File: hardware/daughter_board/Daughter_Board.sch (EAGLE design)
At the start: 60 parts, among them IC1 LMV358MMX, IC2 LMV358MMX, IC3 ATMEGA2560-16AU, IC5 LMV358MMX, IC8 LMV358MMX, IC9 LMV358MMX, Q1 BSS138, Y1 CSTCE16M0V53-R0 16MHZ

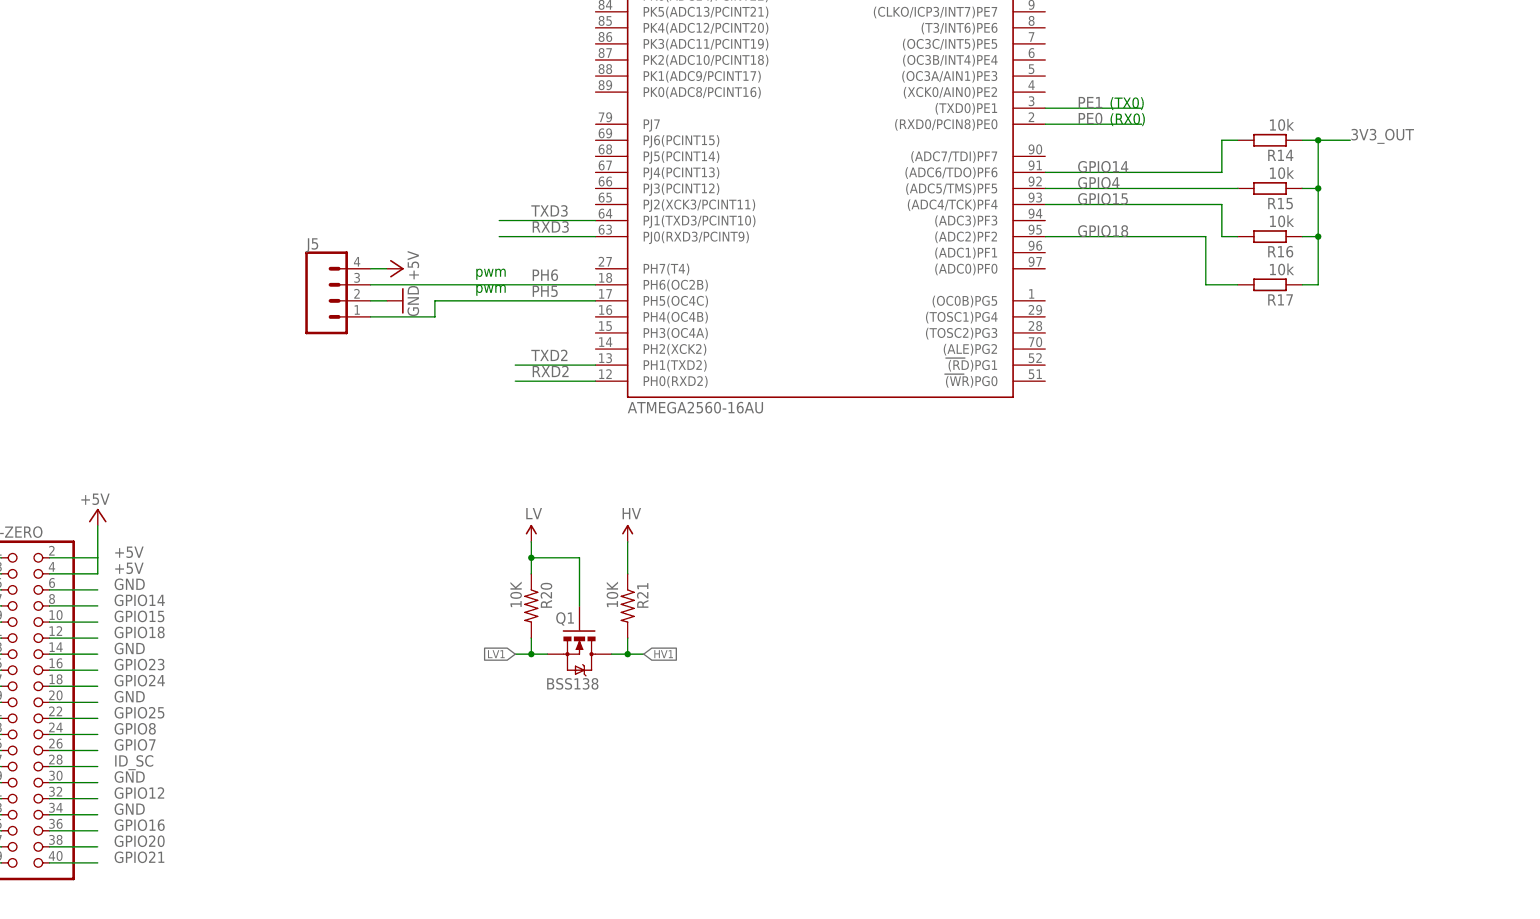
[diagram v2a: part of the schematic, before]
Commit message: level converter and labels
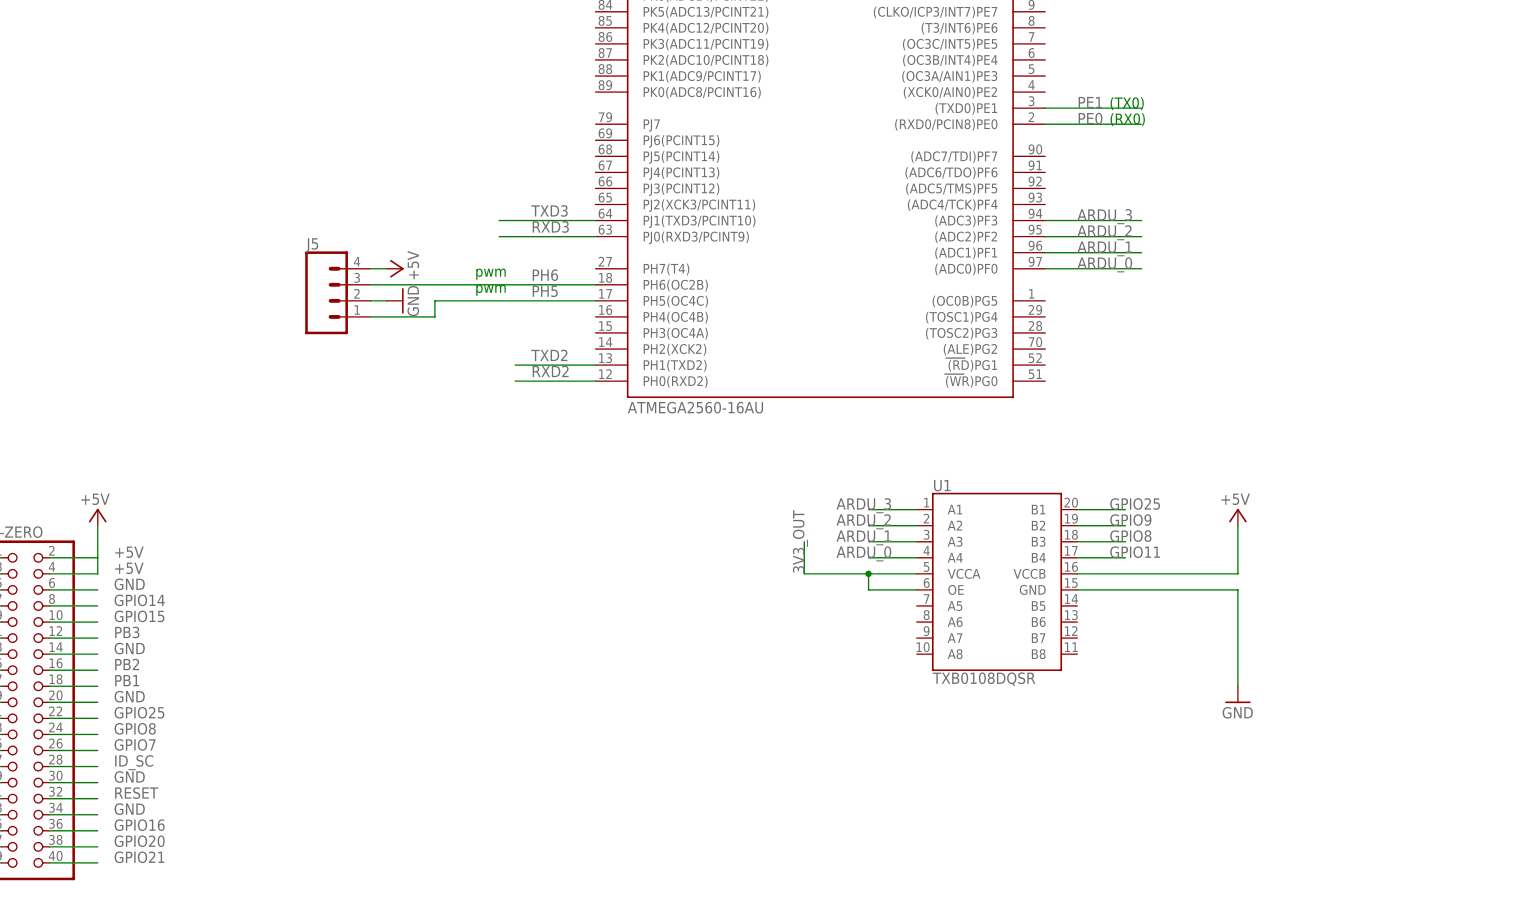
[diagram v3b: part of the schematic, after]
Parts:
- removed Q1: BSS138, SparkFun:MOSFET-NCHANNELSMD
- removed R14, R15, R16, R17: 10k, resistor:R-EU_R0603
- removed R20, R21: 10K, SparkFun:RESISTOR0603-RES
- added U1: TXB0108DQSR, SparkFun-IC-Comms:TXB0108
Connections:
- removed net GPIO12: RPI-ZERO.32
- removed net GPIO18: IC3.(ADC2)PF2, R17.2, RPI-ZERO.12
- removed net GPIO23: RPI-ZERO.16
- removed net GPIO24: RPI-ZERO.18
- removed net HV: R21.1
- removed net HV1: Q1.D, R21.2
- removed net LV: Q1.G, R20.1
- removed net LV1: Q1.S, R20.2
- new net ARDU_0: IC3.(ADC0)PF0, U1.A4
- new net ARDU_1: IC3.(ADC1)PF1, U1.A3
- new net ARDU_2: IC3.(ADC2)PF2, U1.A2
- new net ARDU_3: IC3.(ADC3)PF3, U1.A1
- net +5V: now also U1.VCCB
- net 3V3_OUT: now also U1.OE, U1.VCCA; no longer R14.1, R15.1, R16.1, R17.1
- net GND: now also U1.GND
- net GPIO11: now also U1.B4
- net GPIO14: no longer IC3.(ADC6/TDO)PF6, R14.2
- net GPIO15: no longer IC3.(ADC4/TCK)PF4, R16.2
- net GPIO25: now also U1.B1
- net GPIO4: no longer IC3.(ADC5/TMS)PF5, R15.2
- net GPIO8: now also U1.B3
- net GPIO9: now also U1.B2
- net PB1: now also RPI-ZERO.18
- net PB2: now also RPI-ZERO.16
- net PB3: now also RPI-ZERO.12
- net RESET: now also RPI-ZERO.32

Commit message: some DRC fixes
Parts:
- _: value TS42031-160R-TR-7260 -> TS42
- renumbered RESET to _
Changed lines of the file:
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@@
 <part name="GND20" library="supply1" deviceset="GND" device=""/>
 <part name="R1" library="SmartPrj" deviceset="R-EU_" device="R0603" value="1M"/>
-<part name="RESET" library="SmartPrj" deviceset="TS42" device="" value="TS42031-160R-TR-7260"/>
+<part name="_" library="SmartPrj" deviceset="TS42" device="" value=""/>
 <part name="D3" library="diode" deviceset="DIODE-" device="MINIMELF" value="CD1206-S01575"/>
 <part name="IC1" library="linear" library_urn="urn:adsk.eagle:library:262" deviceset="LMV358?*" device="MM" package3d_urn="urn:adsk.eagle:package:16453/1" technology="X"/>
@@
 <attribute name="VALUE" x="66.675" y="240.792" size="1.778" layer="96" rot="R180"/>
 </instance>
-<instance part="RESET" gate="G$1" x="226.06" y="274.32"/>
+<instance part="_" gate="G$1" x="226.06" y="274.32"/>
 <instance part="D3" gate="G$1" x="256.54" y="287.02" smashed="yes" rot="R90">
 <attribute name="NAME" x="251.9426" y="289.56" size="1.778" layer="95" rot="R270"/>
@@
 <junction x="228.6" y="266.7"/>
 <pinref part="GND12" gate="1" pin="GND"/>
-<pinref part="RESET" gate="G$1" pin="1"/>
-<pinref part="RESET" gate="G$1" pin="2"/>
+<pinref part="_" gate="G$1" pin="1"/>
+<pinref part="_" gate="G$1" pin="2"/>
 </segment>
 <segment>
@@
 <wire x1="228.6" y1="281.94" x2="226.06" y2="281.94" width="0.1524" layer="91"/>
 <wire x1="226.06" y1="281.94" x2="226.06" y2="279.4" width="0.1524" layer="91"/>
-<pinref part="RESET" gate="G$1" pin="4"/>
-<pinref part="RESET" gate="G$1" pin="3"/>
+<pinref part="_" gate="G$1" pin="4"/>
+<pinref part="_" gate="G$1" pin="3"/>
 <wire x1="238.76" y1="276.86" x2="238.76" y2="281.94" width="0.1524" layer="91"/>
 <pinref part="C1" gate="G$1" pin="1"/>

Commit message: Daughter Board v1
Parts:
- removed _: TS42, SmartPrj:TS42
- added S1: MOMENTARY-SWITCH-SPST-SMD-5.2-REDUNDANT, SparkFun-Switches:MOMENTARY-SWITCH-SPST-SMD-5.2-REDUNDANT
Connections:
- net GND: now also S1.1; no longer _.1, _.2
- net RESET: now also S1.2; no longer _.3, _.4
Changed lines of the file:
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@@
 <?xml version="1.0" encoding="utf-8"?>
 <!DOCTYPE eagle SYSTEM "eagle.dtd">
-<eagle version="8.3.2">
+<eagle version="8.4.0">
 <drawing>
 <settings>
@@
 <part name="GND20" library="supply1" deviceset="GND" device=""/>
 <part name="R1" library="SmartPrj" deviceset="R-EU_" device="R0603" value="1M"/>
-<part name="_" library="SmartPrj" deviceset="TS42" device="" value=""/>
 <part name="D3" library="diode" deviceset="DIODE-" device="MINIMELF" value="CD1206-S01575"/>
 <part name="IC1" library="linear" library_urn="urn:adsk.eagle:library:262" deviceset="LMV358?*" device="MM" package3d_urn="urn:adsk.eagle:package:16453/1" technology="X"/>
@@
 <part name="GND10" library="supply1" library_urn="urn:adsk.eagle:library:371" deviceset="GND" device=""/>
 <part name="P+2" library="supply1" deviceset="+5V" device=""/>
+<part name="S1" library="SparkFun-Switches" library_urn="urn:adsk.eagle:library:535" deviceset="MOMENTARY-SWITCH-SPST" device="-SMD-5.2-REDUNDANT" package3d_urn="urn:adsk.eagle:package:40167/1"/>
 </parts>
 <sheets>
@@
 <attribute name="VALUE" x="66.675" y="240.792" size="1.778" layer="96" rot="R180"/>
 </instance>
-<instance part="_" gate="G$1" x="226.06" y="274.32"/>
 <instance part="D3" gate="G$1" x="256.54" y="287.02" smashed="yes" rot="R90">
 <attribute name="NAME" x="251.9426" y="289.56" size="1.778" layer="95" rot="R270"/>
@@
 <attribute name="VALUE" x="207.645" y="81.28" size="1.778" layer="96" rot="R180"/>
 </instance>
+<instance part="S1" gate="G$1" x="228.6" y="274.32" rot="R90"/>
 </instances>
 <busses>
@@
 </segment>
 <segment>
-<wire x1="226.06" y1="269.24" x2="226.06" y2="266.7" width="0.1524" layer="91"/>
-<wire x1="226.06" y1="266.7" x2="228.6" y2="266.7" width="0.1524" layer="91"/>
-<wire x1="228.6" y1="266.7" x2="228.6" y2="269.24" width="0.1524" layer="91"/>
-<wire x1="228.6" y1="266.7" x2="228.6" y2="264.16" width="0.1524" layer="91"/>
-<junction x="228.6" y="266.7"/>
 <pinref part="GND12" gate="1" pin="GND"/>
-<pinref part="_" gate="G$1" pin="1"/>
-<pinref part="_" gate="G$1" pin="2"/>
+<pinref part="S1" gate="G$1" pin="1"/>
+<wire x1="228.6" y1="269.24" x2="228.6" y2="264.16" width="0.1524" layer="91"/>
 </segment>
 <segment>
@@
 <net name="RESET" class="0">
 <segment>
-<wire x1="228.6" y1="279.4" x2="228.6" y2="281.94" width="0.1524" layer="91"/>
-<wire x1="228.6" y1="281.94" x2="226.06" y2="281.94" width="0.1524" layer="91"/>
-<wire x1="226.06" y1="281.94" x2="226.06" y2="279.4" width="0.1524" layer="91"/>
-<pinref part="_" gate="G$1" pin="4"/>
-<pinref part="_" gate="G$1" pin="3"/>
 <wire x1="238.76" y1="276.86" x2="238.76" y2="281.94" width="0.1524" layer="91"/>
 <pinref part="C1" gate="G$1" pin="1"/>
@@
 <wire x1="256.54" y1="281.94" x2="256.54" y2="284.48" width="0.1524" layer="91"/>
 <wire x1="228.6" y1="281.94" x2="238.76" y2="281.94" width="0.1524" layer="91"/>
-<junction x="228.6" y="281.94"/>
 <junction x="238.76" y="281.94"/>
 <pinref part="R13" gate="G$1" pin="2"/>
 <junction x="246.38" y="281.94"/>
-</segment>
-<segment>
+<pinref part="S1" gate="G$1" pin="2"/>
+<wire x1="228.6" y1="281.94" x2="228.6" y2="279.4" width="0.1524" layer="91"/>
+</segment>
+<segment>
